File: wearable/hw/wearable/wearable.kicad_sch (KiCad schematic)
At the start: 110 parts, among them IC1 LM4041CILPR, J2 Conn_02x05_Odd_Even, J8 USBC Charger, SW1 SW_Toggle, U1 LT3042xMSE, U2 BNO080, U3 nRF54L15-QFXX, U4 TPS61040DBV, U5 ADS1299IPAG, U6 nPM1300-QEXX, Y1 32MHz, Y2 32.768kHz, Y3 32.768kHz

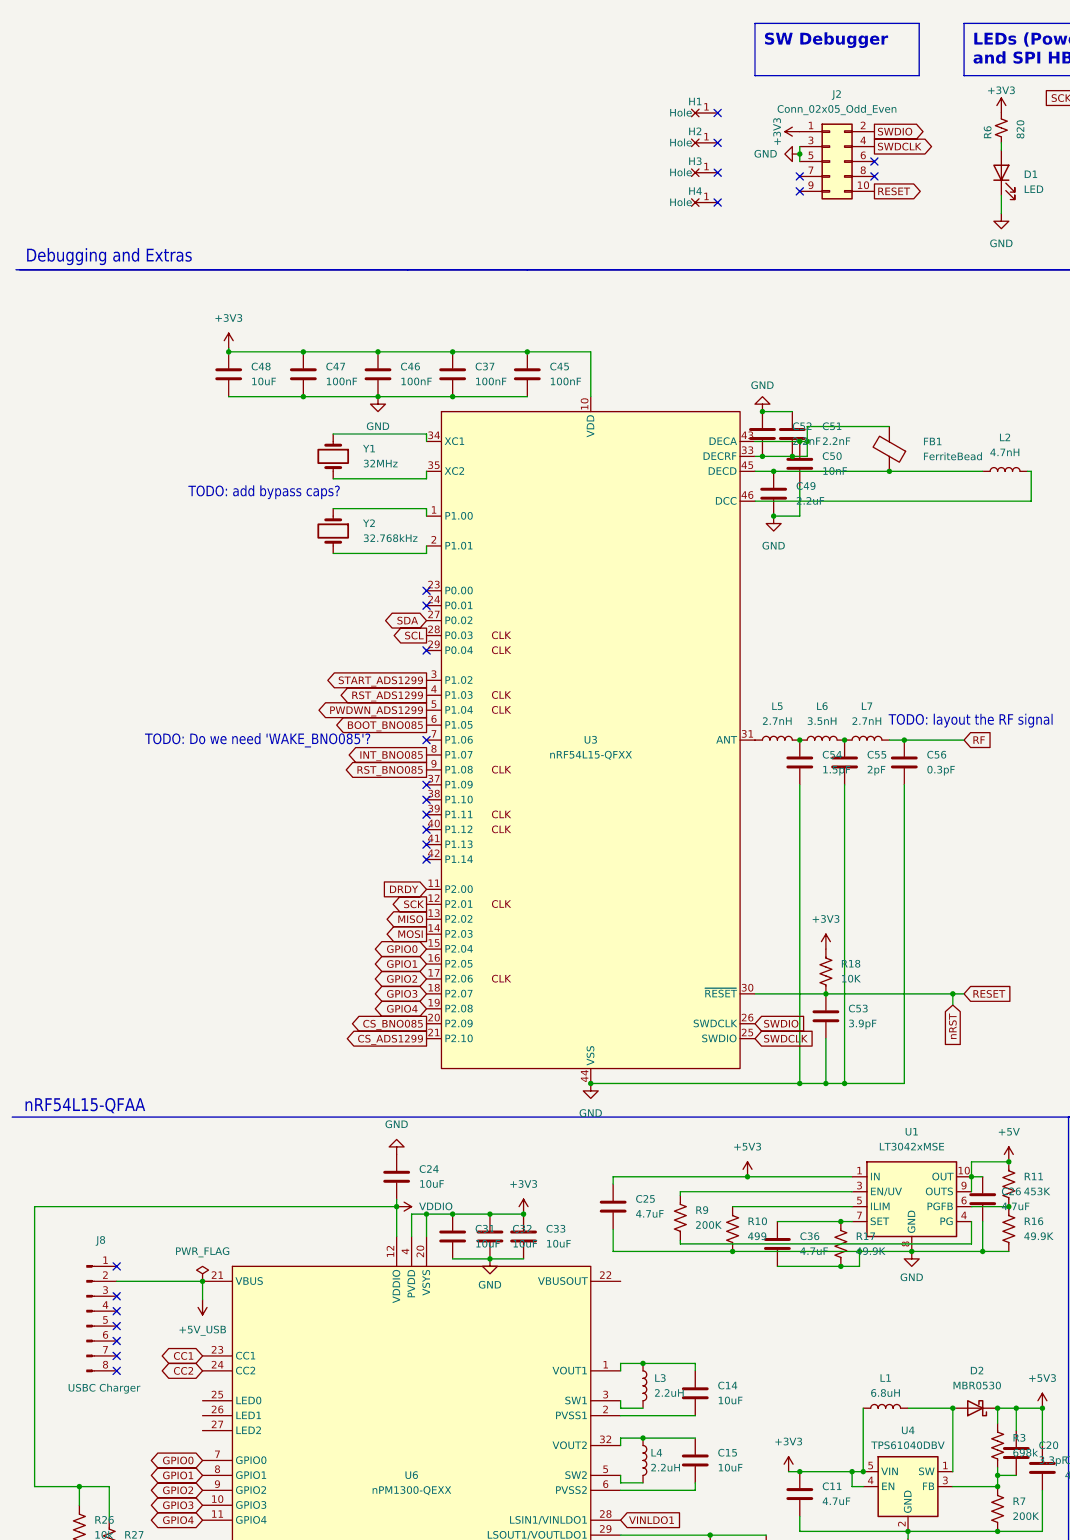
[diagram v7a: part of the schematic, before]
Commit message: Finished routing (mostly) + better testpoints
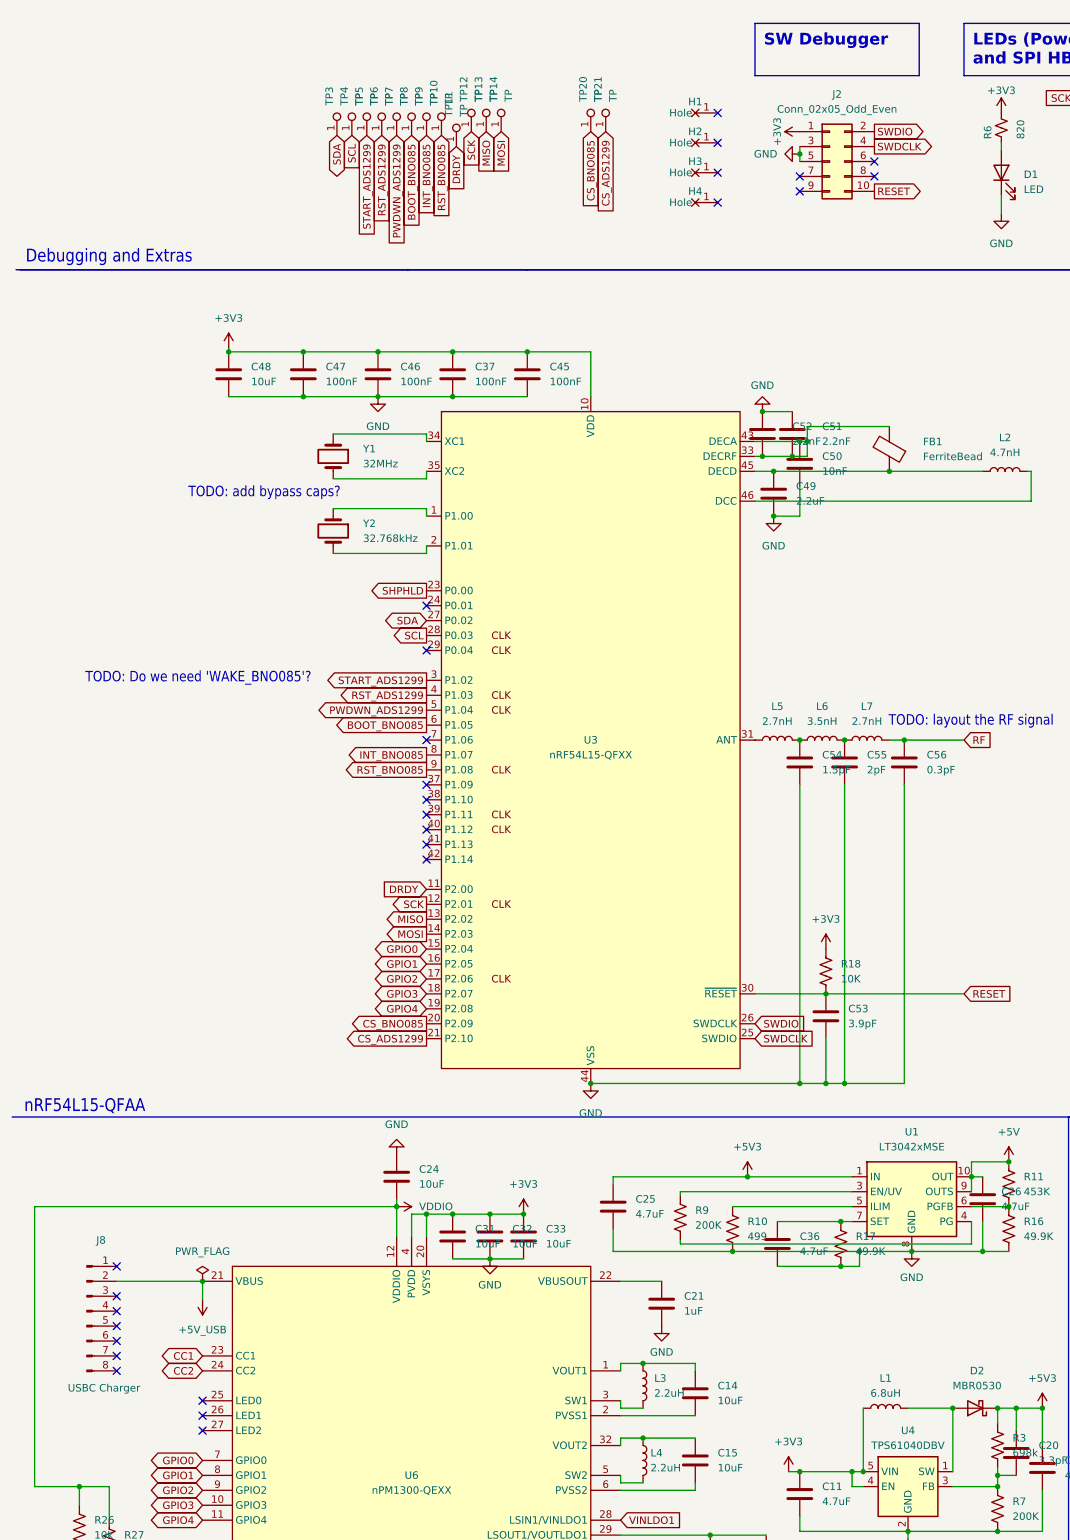
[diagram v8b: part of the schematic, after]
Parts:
- added C21: 1uF, Capacitor_SMD:C_0402_1005Metric, symbol ECE445L:C
- added TP10, TP11, TP12, TP13, TP14, TP20, TP21, TP3, TP4, TP5, TP6, TP7, TP8, TP9: TP, TestPoint:TestPoint_THTPad_D1.0mm_Drill0.5mm, symbol RSLK2:Testpoint_1
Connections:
- net BOOT_BNO085: now also TP8.1 (A)
- net CS_ADS1299: now also TP21.1 (A)
- net CS_BNO085: now also TP20.1 (A)
- net DRDY: now also TP11.1 (A)
- net GND: now also C21.2
- net INT_BNO085: now also TP9.1 (A)
- net MISO: now also TP13.1 (A)
- net MOSI: now also TP14.1 (A)
- net PWDWN_ADS1299: now also TP7.1 (A)
- net RST_ADS1299: now also TP6.1 (A)
- net RST_BNO085: now also TP10.1 (A)
- net SCK: now also TP12.1 (A)
- net SCL: now also TP4.1 (A)
- net SDA: now also TP3.1 (A)
- net SHPHLD: now also U3.23 (P0.00)
- net START_ADS1299: now also TP5.1 (A)
- net at U6.22 (VBUSOUT): now also C21.1
- no-connect marks 31 -> 33
